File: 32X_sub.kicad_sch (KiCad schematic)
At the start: 99 parts, among them IC15 74HC74, IC511 315-5684, IC512 315-5788, IC515 74HC74, IC516 74LS00, T520 TestPoint, T526 TestPoint, T527 TestPoint, T528 TestPoint, T547 TestPoint, T548 TestPoint, T555 TestPoint, T599 AS, X501 *3

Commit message: Start PCB layout.
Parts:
- C444, C554, C556, C557, C558, C559, C560, C561, C562, C564, C565, C566, C567, C568, C569, C570, C571, C572, C573, C574, C575, C576, C577, C578, C579, C580, C588, C589, C590, C591, C592, C593: footprint (none) -> Capacitor_SMD:C_0805_2012Metric
- IC15, IC515, IC516: footprint (none) -> Package_SO:SO-14_3.9x8.65mm_P1.27mm
- IC511, IC512: footprint (none) -> Package_SO:SSOP-32_11.305x20.495mm_P1.27mm
- R23, R45, R511, R512, R513, R514, R515, R516, R517, R518, R519, R520, R521, R522, R524, R525, R526, R527, R528, R529, R530, R531, R532, R533, R534, R535, R536, R537, R539, R540, R541, R544, R547, R549, R558, R559, R560: footprint (none) -> Resistor_SMD:R_0805_2012Metric

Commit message: Save first mock-up before updating footprints.
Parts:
- IC511, IC512: footprint Package_SO:SSOP-32_11.305x20.495mm_P1.27mm -> Neptune:SO-32-0.8mm
- L501: footprint (none) -> Inductor_SMD:L_0805_2012Metric
- R826: renamed from R526; value 75 -> 5.62K
- R827: renamed from R527; value 75 -> 5.62K
- R828: renamed from R528; value 75 -> 5.62K
- R829: renamed from R529; value 75 -> 1.00K
- R830: renamed from R530; value 75 -> 1.00K
- R831: renamed from R531; value 75 -> 1.00K
- renumbered IC15 to IC515
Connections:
- net PCM1: no longer R515.1
- net SR1: no longer C591.1, R512.2
- net 3BP_B renamed VIDEO_B
- net 3BP_CSYNC renamed ~{CSYNC}
- net 3BP_G renamed VIDEO_G
- net 3BP_R renamed VIDEO_R
- net GND renamed GNDA2
- net GNDA2: no longer C575.2, C578.2, C580.1, C592.1, C593.2, CE17.2, IC512.15 (GND), IC512.18 (GND), IC512.26 (GND), IC515.7 (GND), IC516.7 (GND), L501.2, RA501.10 (common), RA501.5 (common), RA502.10 (common), RA502.5 (common)
- new net GND2: C575.2, C578.2, C580.1, C592.1, C593.2, CE17.2, IC512.15 (GND), IC512.18 (GND), IC512.26 (GND), IC515.7 (GND), IC516.7 (GND), L501.2, RA501.10 (common), RA501.5 (common), RA502.10 (common), RA502.5 (common)
- new net PCM0: R515.1
- new net SL1: C591.1, R512.2
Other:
- note added: "NOTE: Resistors for MD video have different values to original 32X because we are taking umamplified RGB from the MD2."

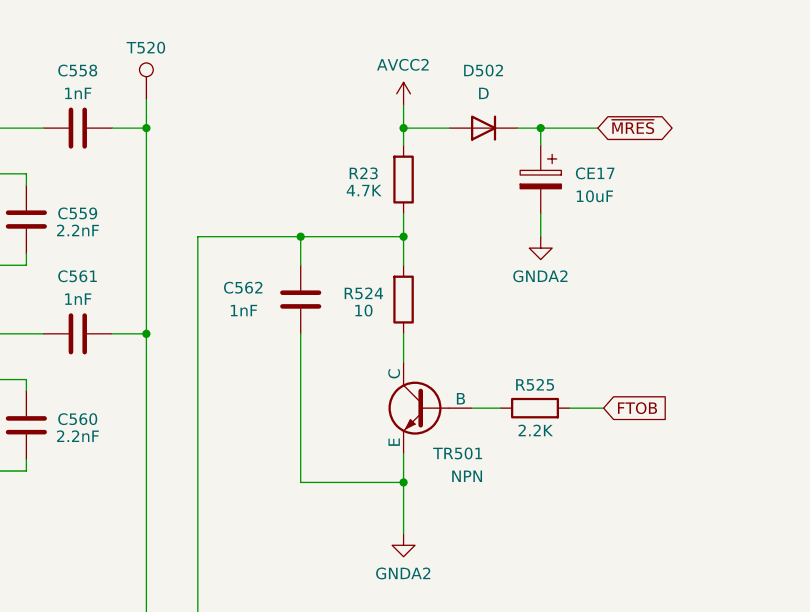
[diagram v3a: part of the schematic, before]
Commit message: Draft new layout with more accurate footprints.
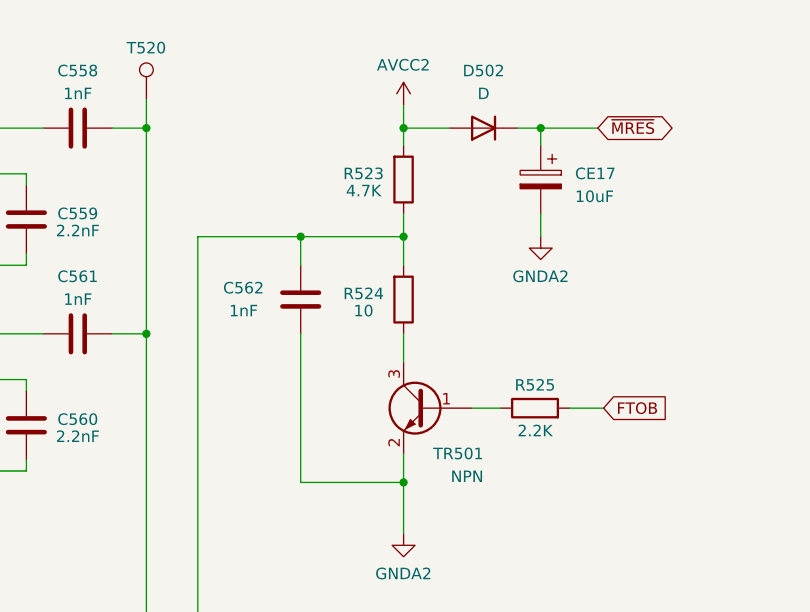
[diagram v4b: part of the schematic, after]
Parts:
- CE17: footprint (none) -> Capacitor_THT:CP_Radial_D5.0mm_P2.50mm
- D502: footprint (none) -> Diode_THT:D_T-1_P5.08mm_Horizontal
- TR501: footprint (none) -> Package_TO_SOT_SMD:SOT-23-3; symbol Simulation_SPICE:NPN -> Device:Q_NPN_BEC
- renumbered R23 to R523
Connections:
- net GNDA2: now also TR501.2 (E); no longer TR501.3 (E)
- net at R524.1: now also TR501.3 (C); no longer TR501.1 (C)
- net at R525.1: now also TR501.1 (B); no longer TR501.2 (B)
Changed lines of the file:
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@@
       (effects (font (size 1.27 1.27)) (justify right))
     )
-    (property "Footprint" "" (at 98.1202 161.925 0)
+    (property "Footprint" "Capacitor_THT:CP_Radial_D5.0mm_P2.50mm" (at 98.1202 161.925 0)
       (effects (font (size 1.27 1.27)) hide)
     )
@@
       (effects (font (size 1.27 1.27)) (justify right))
     )
-    (property "Footprint" "" (at 146.685 102.5652 0)
+    (property "Footprint" "Capacitor_THT:CP_Radial_D5.0mm_P2.50mm" (at 146.685 102.5652 0)
       (effects (font (size 1.27 1.27)) hide)
     )
@@
       (effects (font (size 1.27 1.27)) (justify right))
     )
-    (property "Footprint" "" (at 349.5548 135.89 0)
+    (property "Footprint" "Capacitor_THT:CP_Radial_D5.0mm_P2.50mm" (at 349.5548 135.89 0)
       (effects (font (size 1.27 1.27)) hide)
     )
@@
     )
   )
-  (symbol (lib_id "Simulation_SPICE:NPN") (at 183.515 64.135 0) (mirror y) (unit 1)
+  (symbol (lib_id "Device:Q_NPN_BEC") (at 183.515 64.135 0) (mirror y) (unit 1)
     (in_bom yes) (on_board yes) (dnp no)
     (property "Reference" "TR501" (at 189.865 69.215 0)
@@
       (effects (font (size 1.27 1.27)) (justify left))
     )
-    (property "Footprint" "" (at 120.015 64.135 0)
+    (property "Footprint" "Package_TO_SOT_SMD:SOT-23-3" (at 178.435 61.595 0)
       (effects (font (size 1.27 1.27)) hide)
     )
-    (property "Datasheet" "~" (at 120.015 64.135 0)
+    (property "Datasheet" "~" (at 183.515 64.135 0)
       (effects (font (size 1.27 1.27)) hide)
     )
@@
       (effects (font (size 1.27 1.27)) (justify right))
     )
-    (property "Footprint" "" (at 143.8402 148.59 0)
+    (property "Footprint" "Capacitor_THT:CP_Radial_D5.0mm_P2.50mm" (at 143.8402 148.59 0)
       (effects (font (size 1.27 1.27)) hide)
     )
@@
   (symbol (lib_id "Device:R") (at 180.975 38.735 0) (mirror x) (unit 1)
     (in_bom yes) (on_board yes) (dnp no)
-    (property "Reference" "R23" (at 176.53 38.1 0)
+    (property "Reference" "R523" (at 176.53 38.1 0)
       (effects (font (size 1.27 1.27)))
     )
@@
       (project "Neptune"
         (path "/bcc23b51-b742-4ae5-9dd6-d96a24058944/edde10e2-ce08-4180-9fbe-ab298dfbfa4c"
-          (reference "R23") (unit 1)
+          (reference "R523") (unit 1)
         )
       )
@@
       (effects (font (size 1.27 1.27)))
     )
-    (property "Footprint" "" (at 189.865 33.02 0)
+    (property "Footprint" "Diode_THT:D_T-1_P5.08mm_Horizontal" (at 189.865 33.02 0)
       (effects (font (size 1.27 1.27)) hide)
     )
@@
       (effects (font (size 1.27 1.27)) (justify right))
     )
-    (property "Footprint" "" (at 146.685 110.1852 0)
+    (property "Footprint" "Capacitor_THT:CP_Radial_D5.0mm_P2.50mm" (at 146.685 110.1852 0)
       (effects (font (size 1.27 1.27)) hide)
     )
@@
       (effects (font (size 1.27 1.27)) (justify right))
     )
-    (property "Footprint" "" (at 337.185 122.8852 0)
+    (property "Footprint" "Capacitor_THT:CP_Radial_D5.0mm_P2.50mm" (at 337.185 122.8852 0)
       (effects (font (size 1.27 1.27)) hide)
     )
@@
       (effects (font (size 1.27 1.27)) (justify right))
     )
-    (property "Footprint" "" (at 338.455 49.2252 0)
+    (property "Footprint" "Capacitor_THT:CP_Radial_D5.0mm_P2.50mm" (at 338.455 49.2252 0)
       (effects (font (size 1.27 1.27)) hide)
     )
@@
       (effects (font (size 1.27 1.27)) (justify right))
     )
-    (property "Footprint" "" (at 195.2498 42.545 0)
+    (property "Footprint" "Capacitor_THT:CP_Radial_D5.0mm_P2.50mm" (at 195.2498 42.545 0)
       (effects (font (size 1.27 1.27)) hide)
     )
@@
         )
         (path "/bcc23b51-b742-4ae5-9dd6-d96a24058944/edde10e2-ce08-4180-9fbe-ab298dfbfa4c"
-          (reference "CE1") (unit 1)
+          (reference "CE520") (unit 1)
         )
       )

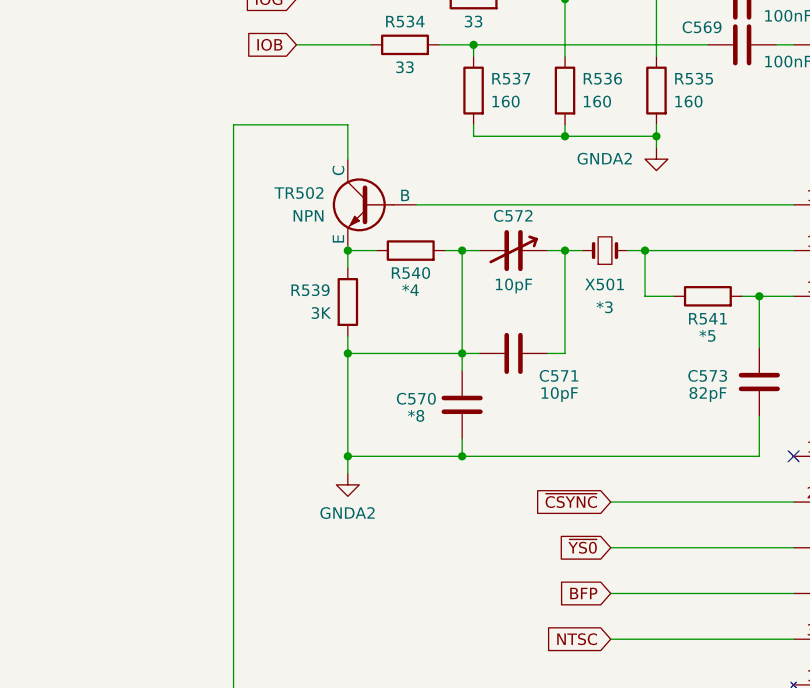
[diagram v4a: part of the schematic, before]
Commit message: First draft "full" layout, bar a few passives.
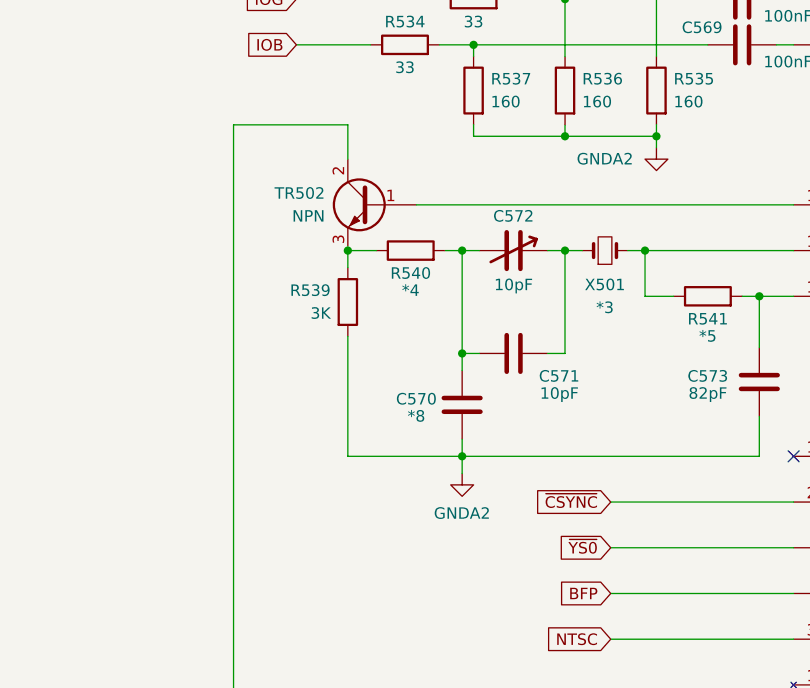
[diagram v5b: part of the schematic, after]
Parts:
- C572: footprint Capacitor_SMD:C_0805_2012Metric -> Capacitor_THT:C_Rect_L7.0mm_W6.5mm_P5.00mm
- TR502: footprint (none) -> Package_TO_SOT_SMD:SOT-23; symbol Simulation_SPICE:NPN -> Device:Q_NPN_BCE
- X501: footprint (none) -> Crystal:Crystal_HC18-U_Vertical
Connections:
- net GNDA2: no longer C570.2, C571.1, C572.2, R540.2
- net at C579.2, C580.2, CE17.1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: now also TR502.2 (C); no longer TR502.1 (C)
- net at IC512.10 (YA): now also TR502.1 (B); no longer TR502.2 (B)
- new net: C570.2, C571.1, C572.2, R540.2
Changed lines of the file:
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@@
   (junction (at 347.98 111.76) (diameter 0) (color 0 0 0 0)
   )
-  (junction (at 246.38 116.84) (diameter 0) (color 0 0 0 0)
-  )
   (junction (at 340.995 127) (diameter 0) (color 0 0 0 0)
   )
@@
   (junction (at 83.82 129.54) (diameter 0) (color 0 0 0 0)
   )
-  (junction (at 246.38 105.41) (diameter 0) (color 0 0 0 0)
-  )
   (junction (at 258.445 33.02) (diameter 0) (color 0 0 0 0)
   )
@@
     (stroke (width 0) (type default))
   )
-  (wire (pts (xy 246.38 103.505) (xy 246.38 105.41))
+  (wire (pts (xy 246.38 103.505) (xy 246.38 116.84))
     (stroke (width 0) (type default))
   )
@@
     (stroke (width 0) (type default))
   )
-  (wire (pts (xy 246.38 105.41) (xy 259.08 105.41))
-    (stroke (width 0) (type default))
-  )
   (wire (pts (xy 227.33 214.63) (xy 231.775 214.63))
     (stroke (width 0) (type default))
@@
     (stroke (width 0) (type default))
   )
-  (wire (pts (xy 246.38 105.41) (xy 246.38 116.84))
-    (stroke (width 0) (type default))
-  )
   (wire (pts (xy 91.44 62.23) (xy 91.44 63.5))
     (stroke (width 0) (type default))
@@
     (stroke (width 0) (type default))
   )
-  (wire (pts (xy 246.38 116.84) (xy 246.38 118.745))
+  (wire (pts (xy 259.08 116.84) (xy 259.08 118.745))
     (stroke (width 0) (type default))
   )
@@
       (effects (font (size 1.27 1.27)))
     )
-    (property "Footprint" "" (at 274.955 93.98 0)
+    (property "Footprint" "Crystal:Crystal_HC18-U_Vertical" (at 274.955 93.98 0)
       (effects (font (size 1.27 1.27)) hide)
     )
@@
     )
   )
-  (symbol (lib_id "Simulation_SPICE:NPN") (at 248.92 88.9 0) (mirror y) (unit 1)
+  (symbol (lib_id "Device:Q_NPN_BCE") (at 248.92 88.9 0) (mirror y) (unit 1)
     (in_bom yes) (on_board yes) (dnp no) (fields_autoplaced)
     (property "Reference" "TR502" (at 243.84 87.63 0)
@@
       (effects (font (size 1.27 1.27)) (justify left))
     )
-    (property "Footprint" "" (at 185.42 88.9 0)
+    (property "Footprint" "Package_TO_SOT_SMD:SOT-23" (at 243.84 86.36 0)
       (effects (font (size 1.27 1.27)) hide)
     )
-    (property "Datasheet" "~" (at 185.42 88.9 0)
+    (property "Datasheet" "~" (at 248.92 88.9 0)
       (effects (font (size 1.27 1.27)) hide)
     )
@@
       (effects (font (size 1.27 1.27)))
     )
-    (property "Footprint" "Capacitor_SMD:C_0805_2012Metric" (at 264.795 93.98 0)
+    (property "Footprint" "Capacitor_THT:C_Rect_L7.0mm_W6.5mm_P5.00mm" (at 264.795 93.98 0)
       (effects (font (size 1.27 1.27)) hide)
     )
@@
     )
   )
-  (symbol (lib_id "32X:GNDA2") (at 246.38 118.745 0) (unit 1)
+  (symbol (lib_id "32X:GNDA2") (at 259.08 118.745 0) (unit 1)
     (in_bom yes) (on_board yes) (dnp no) (fields_autoplaced)
-    (property "Reference" "#PWR0138" (at 246.38 125.095 0)
+    (property "Reference" "#PWR0138" (at 259.08 125.095 0)
       (effects (font (size 1.27 1.27)) hide)
     )
-    (property "Value" "GNDA2" (at 246.38 123.19 0)
+    (property "Value" "GNDA2" (at 259.08 123.19 0)
       (effects (font (size 1.27 1.27)))
     )
-    (property "Footprint" "" (at 246.38 118.745 0)
+    (property "Footprint" "" (at 259.08 118.745 0)
       (effects (font (size 1.27 1.27)) hide)
     )
-    (property "Datasheet" "" (at 246.38 118.745 0)
+    (property "Datasheet" "" (at 259.08 118.745 0)
       (effects (font (size 1.27 1.27)) hide)
     )

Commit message: Fill zones, DRC fixes.
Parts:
- RA501, RA502: footprint (none) -> Neptune:RA_8_2Common
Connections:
- net CTD0: now also RA501.6 (R5); no longer RA501.2 (R2)
- net CTD1: now also RA501.4 (R4); no longer RA501.8 (R7)
- net CTD10: now also RA501.9 (R8); no longer RA502.8 (R7)
- net CTD11: now also RA501.1 (R1); no longer RA502.6 (R5)
- net CTD12: now also RA501.7 (R6); no longer RA502.3 (R3)
- net CTD13: now also RA502.1 (R1); no longer RA502.2 (R2)
- net CTD14: now also RA502.8 (R7); no longer RA502.1 (R1)
- net CTD15: now also RA502.3 (R3); no longer RA501.9 (R8)
- net CTD2: now also RA501.8 (R7); no longer RA502.9 (R8)
- net CTD3: now also RA501.3 (R3); no longer RA502.7 (R6)
- net CTD4: now also RA501.2 (R2); no longer RA502.4 (R4)
- net CTD5: now also RA502.9 (R8); no longer RA501.6 (R5)
- net CTD6: now also RA502.2 (R2); no longer RA501.4 (R4)
- net CTD7: now also RA502.7 (R6); no longer RA501.1 (R1)
- net CTD8: now also RA502.6 (R5); no longer RA501.3 (R3)
- net CTD9: now also RA502.4 (R4); no longer RA501.7 (R6)
- net GND2: no longer C575.2, C578.2, C580.1, CE17.2, IC512.15 (GND), IC512.18 (GND), IC512.26 (GND), L501.2
- net GNDA2: now also C575.2, C578.2, C580.1, CE17.2, IC512.15 (GND), IC512.18 (GND), IC512.26 (GND), L501.2
